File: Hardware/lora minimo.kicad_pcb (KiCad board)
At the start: 2 copper layers, 42 parts, among them J1 USB_B, J2 Conn_01x08, J3 Conn_01x04, Q1 2N7002, Q2 Q_PNP_BEC, SW1 SW_Push, U1 ATSAMD21E18A-MU, U2 MCP73831-2-OT, U3 AP2114H-3.3TRG1, U4 RFM95W-868S2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

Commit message: add netist and pcb
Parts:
- added C4: 4.7 uF, Capacitors_SMD:C_0805_HandSoldering, F.Cu at (188.1, 73.2)
- D3: footprint Diodes_SMD:D_SOD-323F -> Diodes_SMD:D_SOD-323_HandSoldering
- D4: footprint Diodes_SMD:D_SOD-123 -> LEDs:LED_0805_HandSoldering
- J1: footprint Connectors_ec:629105150521 -> USB_WURTH:629105150521
- MODULE1: footprint Rf:L80 -> Rf:QUECTEL_L80-M39
- U2: footprint TO_SOT_Packages_SMD:TSOT-23-5_HandSoldering -> TO_SOT_Packages_SMD:SOT-23-5_HandSoldering
- U3: footprint TO_SOT_Packages_SMD:SOT-223-3_TabPin2 -> TO_SOT_Packages_SMD:SOT-223
- U6: footprint Housings_SOIC:TI_SO-PowerPAD-8 -> Housings_SOIC:Diodes_PSOP-8
- moved U1 109.7 mm to (208.7, 82.5)
- moved J1 100.6 mm to (181.4, 63.4), turned to 0 degrees
- moved R1 69.3 mm to (188.2, 69.5)
- moved AE1 67.6 mm to (173.0, 66.2)
- moved CIN1 67.5 mm to (194.9, 62.6)
- moved R5 65.6 mm to (181.3, 76.5)
- moved MODULE1 65.5 mm to (154.0, 75.6)
- moved H1 60.5 mm to (195.8, 54.4)
- moved H3 56.7 mm to (189.2, 61.4)
- moved RLED1 56.6 mm to (175.2, 79.2)
- moved C2 53.3 mm to (192.7, 67.6)
- moved D3 52.9 mm to (183.5, 57.9)
- moved R9 52.9 mm to (195.0, 60.7)
- moved H4 51.2 mm to (182.4, 72.1)
- moved R3 51.2 mm to (188.6, 55.9)
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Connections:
- D6 pad 2: +BATT -> VBUS
- J2 pad 8: Net-(J2-Pad8) -> VBUS
- R1 pad 1: +BATT -> /VBAT
- U2 pad 3: +BATT -> /VBAT

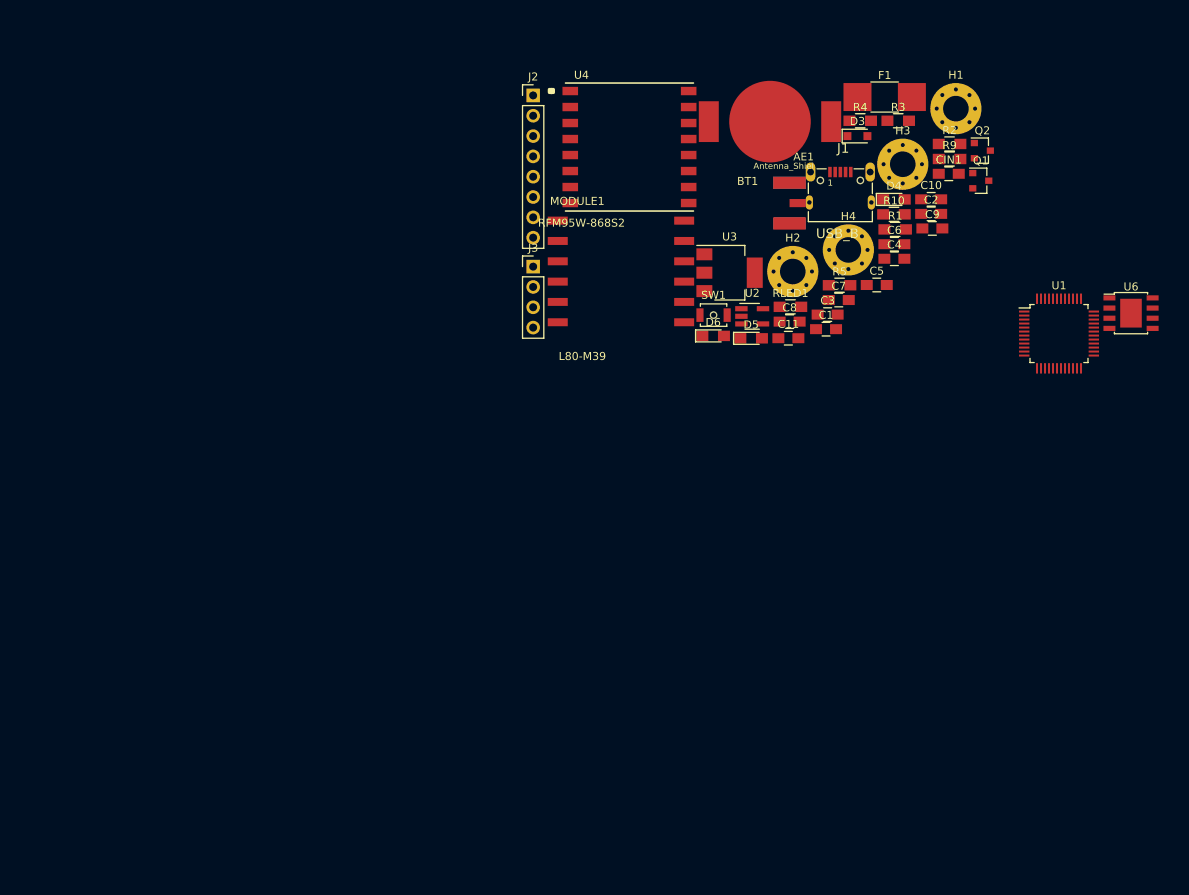
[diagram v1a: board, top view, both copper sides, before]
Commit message: PCB test
pcb design and fingerprint reallocation
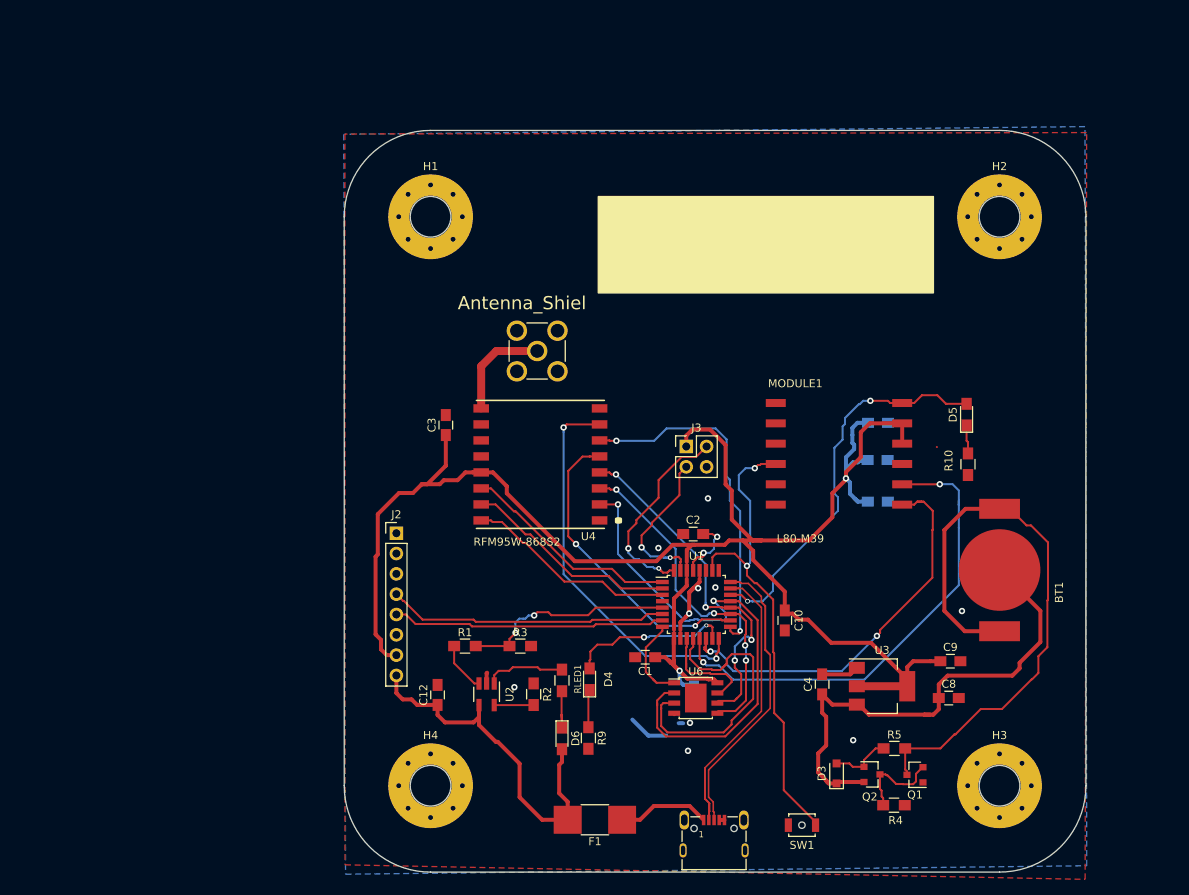
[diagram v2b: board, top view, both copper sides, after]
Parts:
- removed CIN1: 4.7 uF, Capacitors_SMD:C_0805_HandSoldering
- added C12: 4.7 uF, Capacitors_SMD:C_0805_HandSoldering, F.Cu at (131.0, 127.7)
- AE1: footprint Rf:SMA_EDGE -> Rf:AMPHENOL_901-144
- C11, C5, C6, C7: moved to B.Cu
- H1, H2, H3, H4: footprint Mounting_Holes:MountingHole_3.2mm_M3_Pad_Via -> Mounting_Holes:MountingHole_5.3mm_M5_Pad_Via
- J1: footprint USB_WURTH:629105150521 -> Connectors_ec:629105150521
- J2: value Conn_01x08 -> Acelerometer
- J3: value Conn_01x04 -> SWD; footprint Pin_Headers:Pin_Header_Straight_1x04_Pitch2.54mm -> Pin_Headers:Pin_Header_Straight_2x02_Pitch2.54mm
- SW1: value SW_Push -> RESET
- U1: footprint Housings_QFP:TQFP-48_7x7mm_Pitch0.5mm -> Housings_QFP:TQFP-32_7x7mm_Pitch0.8mm
- U3: footprint TO_SOT_Packages_SMD:SOT-223 -> TO_SOT_Packages_SMD:SOT-223-3_TabPin2
- moved F1 97.3 mm to (150.7, 143.3), turned to 180 degrees
- moved R2 86.2 mm to (143.1, 127.6), turned to 90 degrees
- moved R4 85.7 mm to (188.1, 141.5)
- moved R9 85.3 mm to (149.9, 133.1), turned to 270 degrees
- moved H4 84.9 mm to (130.2, 139.1)
- moved J1 82.5 mm to (165.6, 144.4)
- moved R3 80.9 mm to (141.4, 121.6)
- moved D3 79.7 mm to (180.9, 137.5), turned to 90 degrees
- moved Q2 79.2 mm to (185.3, 137.7)
- moved H3 78.6 mm to (201.3, 139.1)
- moved R1 74.9 mm to (134.5, 121.6)
- moved Q1 74.7 mm to (190.7, 137.7), turned to 180 degrees
- moved U6 72.6 mm to (163.3, 128.1)
- moved D4 71.0 mm to (150.1, 125.8), turned to 90 degrees
- moved H1 67.0 mm to (130.2, 67.9)
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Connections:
- D5 pad 2: Net-(D5-Pad2) -> /1PPS
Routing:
- net +3V3: track 0.00 -> 231.2 mm, vias 0 -> 2
- net Net-(BT1-Pad2): track 0.00 -> 74.6 mm
- net /MISO: track 0.00 -> 66.4 mm, vias 0 -> 2
- net +BATT: track 0.00 -> 63.0 mm
- net /Tx: track 0.00 -> 61.0 mm, vias 0 -> 2
- net /RST: track 0.00 -> 60.2 mm, vias 0 -> 2
- net /Rx: track 0.00 -> 52.6 mm, vias 0 -> 2
- net /DIO5: track 0.00 -> 49.6 mm, vias 0 -> 2
- net /1PPS: track 0.00 -> 49.0 mm, vias 0 -> 2
- net VBUS: track 0.00 -> 47.9 mm
- net /SCK: track 0.00 -> 44.7 mm, vias 0 -> 4
- net /RFM_RST: track 0.00 -> 43.9 mm, vias 0 -> 2
- net /MOSI: track 0.00 -> 42.5 mm, vias 0 -> 4
- net /D-: track 0.00 -> 42.5 mm
- net /SS: track 0.00 -> 38.2 mm, vias 0 -> 2
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- added copper zone on B.Cu, net GND
- added copper zone on F.Cu, net GND
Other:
- board outline added: 92.7 x 92.7 mm
- net class Default: trace_width 0.25 -> 0.2
- net class Vcc added: clearance 0.3, trace_width 0.5, via_dia 0.8, via_drill 0.4
- board text added: "GPS LORA TRACK-ZERO"
